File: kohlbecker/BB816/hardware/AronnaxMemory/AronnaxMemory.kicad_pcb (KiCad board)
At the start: 2 copper layers, 19 parts, among them J1 Barrel_Jack_Switch, J2 Conn_02x40_Odd_Even, J3 Conn_02x18_Odd_Even, J4 Conn_02x16_Odd_Even, U1 74LS04, U11 AS6C4008-55PCN, U12 AS6C4008-55PCN, U13 AT28C256-15PC, U2 74LS32, U3 74LS32, U4 74LS32, U5 74LS08, U6 74LS138, U7 74LS138, U8 74LS138

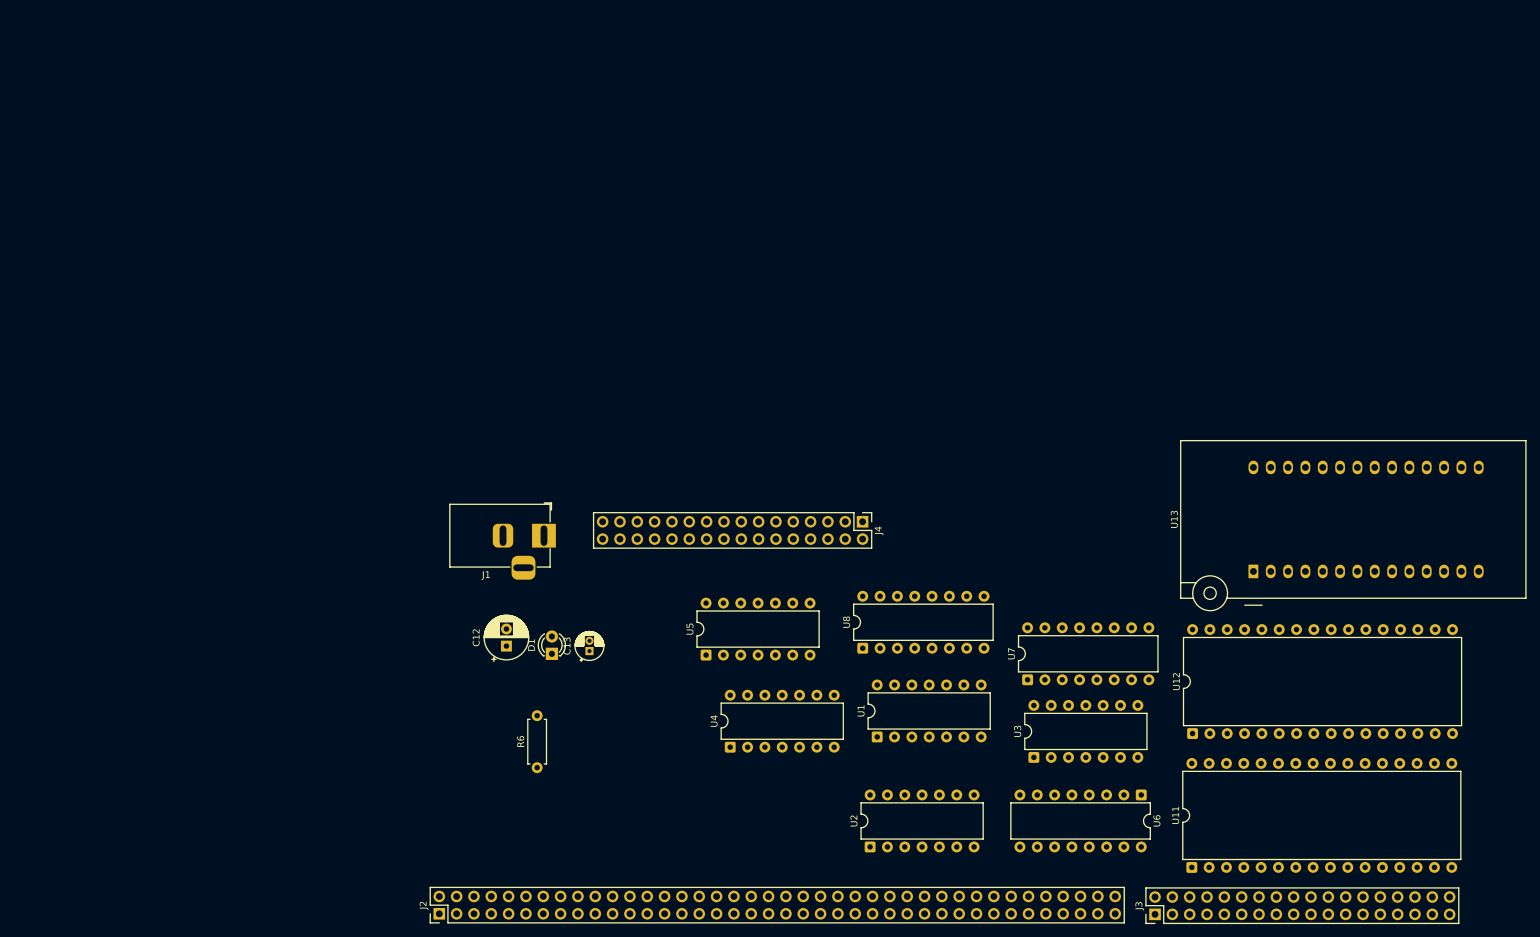
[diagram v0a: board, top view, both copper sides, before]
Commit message: Ready update schematic with added components to breakout
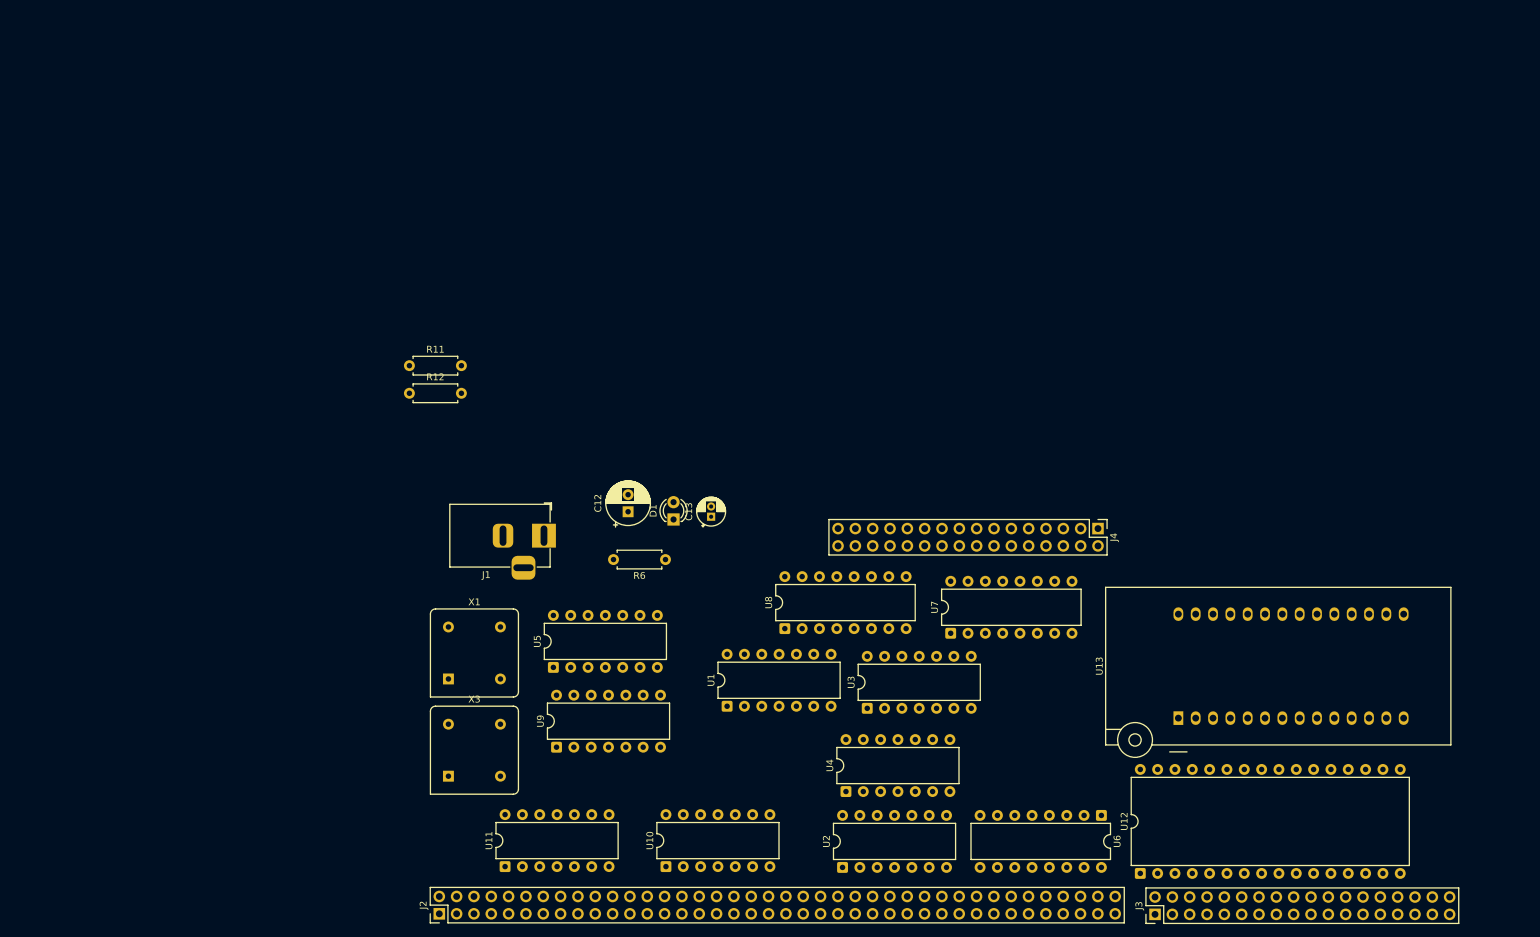
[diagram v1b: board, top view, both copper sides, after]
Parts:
- added R11: 3.3k, Resistor_THT:R_Axial_DIN0207_L6.3mm_D2.5mm_P7.62mm_Horizontal, F.Cu at (58.3, 49.6)
- added R12: 100k, Resistor_THT:R_Axial_DIN0207_L6.3mm_D2.5mm_P7.62mm_Horizontal, F.Cu at (58.3, 53.6)
- added U10: 74AHC125, Package_DIP:DIP-14_W7.62mm, F.Cu at (95.9, 123.0)
- added U9: 74HC74, Package_DIP:DIP-14_W7.62mm, F.Cu at (79.8, 105.5)
- added X1: 8MHz, Oscillator:Oscillator_DIP-8, F.Cu at (64.0, 95.5)
- added X3: 16MHz, Oscillator:Oscillator_DIP-8, F.Cu at (64.0, 109.8)
- U11: value AS6C4008-55PCN -> 74LS32; footprint Package_DIP:DIP-32_W15.24mm -> Package_DIP:DIP-14_W7.62mm
- U4: value 74LS32 -> 74LS08
- U5: value 74LS08 -> 74LS32
- moved U11 100.7 mm to (72.3, 123.0)
- moved R6 35.8 mm to (95.8, 78.0), turned to 180 degrees
- moved J4 34.5 mm to (159.2, 73.5)
- moved C12 26.6 mm to (90.3, 71.0)
- moved C13 26.6 mm to (102.5, 71.7)
- moved D1 26.6 mm to (97.0, 72.1)
- moved U3 25.5 mm to (125.4, 99.8)
- moved U13 24.2 mm to (171.0, 101.2)
- moved U1 22.5 mm to (104.8, 99.5)
- moved U5 22.5 mm to (79.4, 93.8)
- moved U12 21.9 mm to (165.4, 124.0)
- moved U4 18.2 mm to (122.3, 112.0)
- moved U7 13.2 mm to (137.6, 88.8)
- moved U8 11.8 mm to (113.3, 88.1)
- moved U6 6.57 mm to (159.7, 115.5)
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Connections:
- J4 pad 1: ~{MEG0} -> ~{MEG0_LO}
- J4 pad 3: MEG0 -> MEG0_LO
- J4 pad 5: ~{MEG0_HI} -> unconnected-(J4-Pin_5-Pad5)
- J4 pad 7: ~{MEG0_LO} -> unconnected-(J4-Pin_7-Pad7)
- U1 pad 1: /A19 -> ~{MEG0_LO}
- U1 pad 12: MEG0 -> Net-(X3-EN)
- U1 pad 13: ~{MEG0} -> /E
- U1 pad 2: Net-(U1-Pad2) -> MEG0_LO
- U1 pad 3: /A15 -> /E
- U1 pad 5: /E -> /A15
- U11 pad 1: /A18 -> /16MHz
- U11 pad 10: /A2 -> (no net)
- U11 pad 11: /A1 -> (no net)
- U11 pad 12: /A0 -> (no net)
- U11 pad 13: /D0 -> (no net)
- U11 pad 14: /D1 -> (no net)
- U11 pad 2: /A16 -> /8MHz
- U11 pad 3: /A14 -> Net-(U9B-C)
- U11 pad 4: /A12 -> (no net)
- U11 pad 5: /A7 -> (no net)
- U11 pad 6: /A6 -> (no net)
- U11 pad 7: /A5 -> (no net)
- U11 pad 8: /A4 -> (no net)
- U11 pad 9: /A3 -> (no net)
- U12 pad 22: ~{MEG0LO} -> ~{MEG0_LO}
- U2 pad 11: ~{MEG0HI} -> ~{MEG0_LO}
- U2 pad 12: ~{MEG0} -> Net-(U2-Pad12)
- U2 pad 13: Net-(U1-Pad2) -> /A19
- U2 pad 8: ~{MEG0} -> Net-(U2-Pad12)
- U3 pad 1: ~{MEG0} -> Net-(U1-Pad4)
- U3 pad 10: ~{BANK0_HI} -> /A15
- U3 pad 11: ~{BANK0_LO} -> Net-(U12-OE#)
- U3 pad 12: /~{BANK0} -> Net-(U3-Pad12)
- U3 pad 13: /A15 -> Net-(U1-Pad10)
- U3 pad 2: /A19 -> ~{BANK0_HI}
- U3 pad 3: ~{MEG0LO} -> ~{ROM_OE}
- U3 pad 4: Net-(U1-Pad4) -> Net-(U1-Pad6)
- U3 pad 8: ~{ROM_OE} -> ~{BANK0_LO}
- U3 pad 9: Net-(U1-Pad6) -> /~{BANK0}
- U4 pad 1: Net-(U4-Pad1) -> Net-(U1-Pad8)
- U4 pad 2: Net-(U1-Pad10) -> /E
- U4 pad 3: Net-(U12-OE#) -> Net-(U3-Pad12)
- U5 pad 1: Net-(U1-Pad8) -> (no net)
- U5 pad 2: /E -> (no net)
- U5 pad 3: Net-(U4-Pad1) -> (no net)

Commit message: getting ready to add VPB rewrite
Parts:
- removed J4: Conn_02x16_Odd_Even, Connector_PinHeader_2.54mm:PinHeader_2x16_P2.54mm_Vertical
- removed R11: 3.3k, Resistor_THT:R_Axial_DIN0207_L6.3mm_D2.5mm_P7.62mm_Horizontal
- removed R12: 100k, Resistor_THT:R_Axial_DIN0207_L6.3mm_D2.5mm_P7.62mm_Horizontal
- removed U10: 74AHC125, Package_DIP:DIP-14_W7.62mm
- removed U11, U5: 74LS32, Package_DIP:DIP-14_W7.62mm
- removed U9: 74HC74, Package_DIP:DIP-14_W7.62mm
- removed X1: 8MHz, Oscillator:Oscillator_DIP-8
- removed X3: 16MHz, Oscillator:Oscillator_DIP-8
- added C1: 100nF, Capacitor_THT:C_Disc_D3.4mm_W2.1mm_P2.50mm, F.Cu at (46.5, 76.0)
- added C2: 100nF, Capacitor_THT:C_Disc_D3.4mm_W2.1mm_P2.50mm, F.Cu at (78.8, 112.1)
- added C3: 100nF, Capacitor_THT:C_Disc_D3.4mm_W2.1mm_P2.50mm, F.Cu at (78.4, 68.5)
- added C4: 100nF, Capacitor_THT:C_Disc_D3.4mm_W2.1mm_P2.50mm, F.Cu at (119.0, 88.4)
- added C5: 100nF, Capacitor_THT:C_Disc_D3.4mm_W2.1mm_P2.50mm, F.Cu at (111.2, 68.0)
- added C6: 100nF, Capacitor_THT:C_Disc_D3.4mm_W2.1mm_P2.50mm, F.Cu at (78.1, 93.5)
- added C7: 100nF, Capacitor_THT:C_Disc_D3.4mm_W2.1mm_P2.50mm, F.Cu at (80.5, 80.9)
- added C8: 100nF, Capacitor_THT:C_Disc_D3.4mm_W2.1mm_P2.50mm, F.Cu at (105.8, 89.0)
- added C9: 100nF, Capacitor_THT:C_Disc_D3.4mm_W2.1mm_P2.50mm, F.Cu at (105.7, 68.0)
- added H1: MountingHole_Pad, MountingHole:MountingHole_3.2mm_M3_Pad, F.Cu at (30.5, 71.1)
- added H2: MountingHole_Pad, MountingHole:MountingHole_3.2mm_M3_Pad, F.Cu at (172.7, 71.1)
- added J5: I/O ~{CS}, Connector_PinHeader_2.54mm:PinHeader_2x10_P2.54mm_Vertical, F.Cu at (75.0, 68.4)
- added REF**: Symbol_Barrel_Polarity, Symbol:Symbol_Barrel_Polarity, F.Cu at (32.2, 88.9)
- J2, J3: moved to B.Cu
- U6, U7: value 74LS138 -> 74LS32; footprint Package_DIP:DIP-16_W7.62mm -> Package_DIP:DIP-14_W7.62mm
- moved U6 76.1 mm to (98.1, 70.9), turned to 0 degrees
- moved U12 65.6 mm to (114.1, 83.2)
- moved U8 63.9 mm to (49.6, 83.6)
- moved D1 57.2 mm to (41.8, 87.3), turned to 0 degrees
- moved C13 55.6 mm to (47.0, 68.9), turned to 0 degrees
- moved U4 55.3 mm to (78.3, 78.5)
- moved C12 53.3 mm to (37.1, 71.1), turned to 0 degrees
- moved U13 52.6 mm to (119.0, 109.3)
- moved R6 52.5 mm to (43.4, 75.0), turned to 90 degrees
- moved U3 48.1 mm to (78.1, 90.9)
- moved U2 43.0 mm to (78.8, 122.2)
- moved U7 39.9 mm to (97.9, 91.9), turned to 0 degrees
- moved J1 39.1 mm to (39.4, 80.6)
- moved J3 35.6 mm to (132.1, 127.0), turned to -90 degrees
- moved J2 34.8 mm to (27.9, 127.0), turned to -90 degrees
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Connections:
- net ~{ROM_OE} renamed /~{ROM_OE}
- J3 pad 11: /A4 -> /AA4
- J3 pad 13: /A3 -> /AA3
- J3 pad 15: /A2 -> /AA2
- J3 pad 17: /A1 -> /AA1
- U1 pad 1: ~{MEG0_LO} -> /E
- U1 pad 11: ~{PAGE1} -> /A19
- U1 pad 12: Net-(X3-EN) -> Net-(U1-Pad12)
- U1 pad 13: /E -> ~{PAGE1}
- U1 pad 2: MEG0_LO -> Net-(U1-Pad2)
- U1 pad 3: /E -> /~{BANK0_HI}
- U1 pad 8: Net-(U1-Pad8) -> unconnected-(U1-Pad8)
- U1 pad 9: ~{BANK0_HI} -> GND
- U12 pad 22: ~{MEG0_LO} -> /~{MEG0_LO}
- U13 pad 20: ~{BANK0_HI} -> /~{BANK0_HI}
- U2 pad 10: Net-(U2-Pad10) -> /A19
- U2 pad 11: ~{MEG0_LO} -> Net-(U2-Pad11)
- U2 pad 13: /A19 -> Net-(U2-Pad13)
- U2 pad 3: Net-(U2-Pad3) -> Net-(U2-Pad13)
- U2 pad 6: Net-(U2-Pad10) -> Net-(U2-Pad12)
- U2 pad 8: Net-(U2-Pad12) -> /~{MEG0_LO}
- U2 pad 9: Net-(U2-Pad3) -> Net-(U2-Pad11)
- U3 pad 1: Net-(U1-Pad4) -> Net-(U1-Pad2)
- U3 pad 13: Net-(U1-Pad10) -> Net-(U1-Pad12)
- U3 pad 2: ~{BANK0_HI} -> /~{BANK0_HI}
- U3 pad 6: ~{BANK0_HI} -> /~{BANK0_HI}
- U3 pad 8: ~{BANK0_LO} -> /~{BANK0_LO}
- U4 pad 1: Net-(U1-Pad8) -> GND
- U4 pad 10: (no net) -> GND
- U4 pad 11: (no net) -> unconnected-(U4-Pad11)
- U4 pad 12: (no net) -> GND
- U4 pad 13: (no net) -> GND
- U4 pad 2: /E -> GND
- U4 pad 3: Net-(U3-Pad12) -> unconnected-(U4-Pad3)
- U4 pad 4: (no net) -> Net-(U1-Pad4)
- U4 pad 5: (no net) -> /E
- U4 pad 6: (no net) -> Net-(U3-Pad12)
- U4 pad 8: (no net) -> unconnected-(U4-Pad8)
- U4 pad 9: (no net) -> GND
- U6 pad 1: /A11 -> /~{BANK0_LO}
- U6 pad 10: unconnected-(U6-O5-Pad10) -> Net-(U6-Pad10)
- U6 pad 11: unconnected-(U6-O4-Pad11) -> ~{MEG0_HI}
- U6 pad 12: unconnected-(U6-O3-Pad12) -> Net-(U1-Pad10)
- U6 pad 13: unconnected-(U6-O2-Pad13) -> Net-(U2-Pad11)
- U6 pad 14: unconnected-(U6-O1-Pad14) -> VCC
- U6 pad 2: /A12 -> /A8
- U6 pad 3: /A13 -> Net-(U6-Pad10)
- U6 pad 4: ~{BANK0_LO} -> /A9
- U6 pad 5: /A14 -> /A10
- U6 pad 6: VCC -> Net-(U6-Pad6)
- U6 pad 7: unconnected-(U6-O7-Pad7) -> GND
- U6 pad 8: unconnected-(U6-GND-Pad8) -> Net-(U6-Pad8)
- U6 pad 9: unconnected-(U6-O6-Pad9) -> Net-(U6-Pad6)
- U7 pad 1: /A8 -> /A11
- U7 pad 10: unconnected-(U7-O5-Pad10) -> Net-(U7-Pad10)
- U7 pad 11: unconnected-(U7-O4-Pad11) -> Net-(U7-Pad10)
- U7 pad 12: unconnected-(U7-O3-Pad12) -> Net-(U7-Pad12)
- U7 pad 13: unconnected-(U7-O2-Pad13) -> Net-(U7-Pad13)
- U7 pad 14: ~{PAGE1} -> VCC
- U7 pad 2: /A9 -> /A12
- U7 pad 3: /A10 -> Net-(U7-Pad13)
- U7 pad 4: Net-(U6-O0) -> /A13
- U7 pad 5: /A11 -> /A14
- U7 pad 6: VCC -> Net-(U7-Pad12)
- U7 pad 7: unconnected-(U7-O7-Pad7) -> GND
- U7 pad 8: unconnected-(U7-GND-Pad8) -> ~{PAGE1}
- U7 pad 9: unconnected-(U7-O6-Pad9) -> Net-(U6-Pad8)
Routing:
- added copper zone on In1.Cu, net GND
- added copper zone on In2.Cu, net GND
- added copper zone on B.Cu, net VCC
- added copper zone on F.Cu, net VCC
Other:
- board outline added: 152.4 x 64.8 mm
- copper layers 2 -> 4
- board text added: "+"
- board text added: "+5V"
- board text added: "-"
- board text added: "5V"
- board text added: "A0"
- board text added: "A1"
- board text added: "A10"
- board text added: "A11"
- board text added: "A12"
- board text added: "A13"
- board text added: "A14"
- board text added: "A15"
- board text added: "A16"
- board text added: "A17"
- board text added: "A18"
- board text added: "A19"
- board text added: "A2"
- board text added: "A20"
- board text added: "A21"
- board text added: "A22"
- board text added: "A23"
- board text added: "A3"
- board text added: "A4"
- board text added: "A5"
- board text added: "A6"
- board text added: "A7"
- board text added: "A8"
- board text added: "A9"
- board text added: "BE"
- board text added: "CLK"
- board text added: "CLK_SRC"
- board text added: "D0"
- board text added: "D1"
- board text added: "D2"
- board text added: "D3"
- board text added: "D4"
- board text added: "D5"
- board text added: "D6"
- board text added: "D7"
- board text added: "E"
- board text added: "GND"
- board text added: "M"
- board text added: "RDY_IN"
- board text added: "RST"
- board text added: "R~{W}"
- board text added: "SYNC"
- board text added: "VA"
- board text added: "X"
- board text added: "~{00}"
- board text added: "~{20}"
- board text added: "~{40}"
- board text added: "~{512K_1}"
- board text added: "~{60}"
- board text added: "~{80}"
- board text added: "~{A0}"
- board text added: "~{ABORT}"
- board text added: "~{BANK0}"
- board text added: "~{C0}"
- board text added: "~{CLK"
- board text added: "~{CLK_EN}"
- board text added: "~{E0}"
- board text added: "~{IRQ}"
- board text added: "~{ML}"
- board text added: "~{MR}⎒"
- board text added: "~{NMI}"
- board text added: "~{PAGE_1}"
- board text added: "~{RD}"
- board text added: "~{RST}"
- board text added: "~{VP}"
- board text added: "~{WAI}"
- board text added: "~{WR}"

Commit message: Memory
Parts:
- added J9: Vector Rewrite, Connector_PinHeader_2.54mm:PinHeader_2x11_P2.54mm_Vertical, B.Cu at (127.1, 118.0)
- moved U1 36.6 mm to (87.9, 68.4), turned to 0 degrees
- moved C6 32.2 mm to (98.0, 68.2), turned to -90 degrees
- moved C9 28.3 mm to (88.0, 90.2), turned to -90 degrees
- moved U6 27.9 mm to (90.9, 97.8), turned to 90 degrees
- moved C13 27.5 mm to (39.1, 95.3)
- moved R6 27.5 mm to (35.5, 101.3)
- moved C12 27.5 mm to (29.2, 97.4)
- moved U3 26.8 mm to (104.6, 86.8)
- moved U4 26.4 mm to (104.6, 75.8)
- moved C3 23.3 mm to (101.7, 68.0), turned to -90 degrees
- moved C8 21.9 mm to (88.0, 101.8), turned to -90 degrees
- moved C7 21.2 mm to (101.7, 79.2), turned to -90 degrees
- moved U7 19.1 mm to (90.9, 109.7), turned to 90 degrees
- moved U13 15.9 mm to (134.9, 109.1)
- moved C4 15.7 mm to (134.7, 88.8)
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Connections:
- U3 pad 1: Net-(U1-Pad2) -> Net-(U1-Pad6)
- U3 pad 2: /~{BANK0_HI} -> /~{BANK0}
- U3 pad 3: /~{ROM_OE} -> /~{BANK0_HI}
- U3 pad 4: Net-(U1-Pad6) -> Net-(U1-Pad2)
- U3 pad 5: /~{BANK0} -> /~{BANK0_HI}
- U3 pad 6: /~{BANK0_HI} -> /~{ROM_OE}
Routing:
- net /A10: track 0.00 -> 88.7 mm, vias 0 -> 1
- net /A14: track 0.00 -> 82.0 mm, vias 0 -> 1
- net /~{MEG0_LO}: track 0.00 -> 79.0 mm
- net /A9: track 0.00 -> 75.1 mm
- net /A11: track 0.00 -> 74.5 mm, vias 0 -> 1
- net /A13: track 0.00 -> 67.8 mm, vias 0 -> 1
- net /A17: track 0.00 -> 66.6 mm
- net /D3: track 0.00 -> 65.8 mm
- net /A8: track 0.00 -> 62.5 mm
- net /D4: track 0.00 -> 60.4 mm
- net /D7: track 0.00 -> 60.2 mm
- net /D5: track 0.00 -> 60.0 mm
- net /D6: track 0.00 -> 59.9 mm
- net /A0: track 0.00 -> 53.7 mm
- net /E: track 0.00 -> 52.6 mm
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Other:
- board text added: "~{$80000}"
- board text added: "~{0100}"
- board text removed: "~{512K_1}"
- board text removed: "~{PAGE_1}"

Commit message: Cleanup
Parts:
- removed C6, C8: 100nF, Capacitor_THT:C_Disc_D3.4mm_W2.1mm_P2.50mm
- removed U2, U7: 74LS32, Package_DIP:DIP-14_W7.62mm
- removed U8: 74LS138, Package_DIP:DIP-16_W7.62mm
- added C10: 100nF, Capacitor_THT:C_Disc_D3.4mm_W2.1mm_P2.50mm, F.Cu at (121.5, 88.9)
- added C11: 100nF, Capacitor_THT:C_Disc_D3.4mm_W2.1mm_P2.50mm, F.Cu at (128.2, 67.5)
- added U10: 74HC30, Package_DIP:DIP-14_W7.62mm, F.Cu at (115.3, 91.8)
- added U9: CD4072B, Package_DIP:DIP-14_W7.62mm, F.Cu at (91.4, 119.6)
- moved C1 60.1 mm to (112.8, 91.5)
- moved C2 51.5 mm to (110.4, 67.4), turned to 180 degrees
- moved U1 27.6 mm to (102.7, 91.7)
- moved U6 27.3 mm to (90.6, 70.5), turned to 0 degrees
- moved C3 20.8 mm to (122.5, 67.4), turned to 180 degrees
- moved C9 19.6 mm to (91.3, 109.5), turned to 0 degrees
- moved U3 19.3 mm to (114.8, 70.5), turned to 0 degrees
- moved C7 12.3 mm to (98.3, 67.4), turned to 180 degrees
- moved J5 11.1 mm to (74.8, 76.1)
- moved U4 5.65 mm to (102.7, 70.5), turned to 0 degrees
- moved U12 1.48 mm to (128.4, 85.1)
- moved C5 1.48 mm to (125.6, 69.9)
- moved C4 1.28 mm to (135.1, 87.6), turned to 180 degrees
- moved U13 0.44 mm to (135.2, 108.8)
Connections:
- net /~{WR} renamed ~{WR}
- J5 pad 10: ~{0xA0} -> unconnected-(J5-Pin_10-Pad10)
- J5 pad 12: ~{0x80} -> unconnected-(J5-Pin_12-Pad12)
- J5 pad 14: ~{0x60} -> unconnected-(J5-Pin_14-Pad14)
- J5 pad 16: ~{0x40} -> unconnected-(J5-Pin_16-Pad16)
- J5 pad 18: ~{0x20} -> unconnected-(J5-Pin_18-Pad18)
- J5 pad 20: ~{0x00} -> unconnected-(J5-Pin_20-Pad20)
- J5 pad 6: ~{0xE0} -> unconnected-(J5-Pin_6-Pad6)
- J5 pad 8: ~{0xCO} -> unconnected-(J5-Pin_8-Pad8)
- J9 pad 15: Net-(J9-Pin_15) -> GND
- J9 pad 17: Net-(J9-Pin_15) -> GND
- J9 pad 19: Net-(J9-Pin_15) -> GND
- J9 pad 21: Net-(J9-Pin_15) -> GND
- U1 pad 1: /E -> /A15
- U1 pad 11: /A19 -> /E
- U1 pad 13: ~{PAGE1} -> ~{BANK0_HI}
- U1 pad 2: Net-(U1-Pad2) -> /~{A15}
- U1 pad 3: /~{BANK0_HI} -> PAGE1
- U1 pad 4: Net-(U1-Pad4) -> ~{PAGE1}
- U1 pad 5: /A15 -> GND
- U1 pad 6: Net-(U1-Pad6) -> unconnected-(U1-Pad6)
- U1 pad 8: unconnected-(U1-Pad8) -> /~{A19}
- U1 pad 9: GND -> /A19
- U12 pad 22: /~{MEG0_LO} -> ~{MEG0_LO}
- U12 pad 24: Net-(U12-OE#) -> ~{MEG0_LO_OE}
- U13 pad 20: /~{BANK0_HI} -> ~{BANK0_HI}
- U13 pad 22: /~{ROM_OE} -> unconnected-(U13-~{OE}-Pad22)
- U3 pad 1: Net-(U1-Pad6) -> /~{A15}
- U3 pad 10: /A15 -> PAGE1
- U3 pad 11: Net-(U12-OE#) -> /~{BANK0_LO}
- U3 pad 12: Net-(U3-Pad12) -> /~{BANK0}
- U3 pad 13: Net-(U1-Pad12) -> /A15
- U3 pad 3: /~{BANK0_HI} -> ~{BANK0_HI}
- U3 pad 4: Net-(U1-Pad2) -> Net-(U1-Pad10)
- U3 pad 5: /~{BANK0_HI} -> ~{BANK0_HI}
- U3 pad 6: /~{ROM_OE} -> ~{ROM_OE}
- U3 pad 8: /~{BANK0_LO} -> ~{MEG0_LO_OE}
- U3 pad 9: /~{BANK0} -> Net-(U3-Pad9)
- U4 pad 11: unconnected-(U4-Pad11) -> Net-(U3-Pad9)
- U4 pad 12: GND -> Net-(U1-Pad12)
- U4 pad 13: GND -> /E
- U4 pad 4: Net-(U1-Pad4) -> GND
- U4 pad 5: /E -> GND
- U4 pad 6: Net-(U3-Pad12) -> unconnected-(U4-Pad6)
- U6 pad 1: /~{BANK0_LO} -> /~{MEG0}
- U6 pad 10: Net-(U6-Pad10) -> GND
- U6 pad 12: Net-(U1-Pad10) -> /~{A19}
- U6 pad 13: Net-(U2-Pad11) -> /~{MEG0}
- U6 pad 2: /A8 -> /A19
- U6 pad 3: Net-(U6-Pad10) -> ~{MEG0_LO}
- U6 pad 4: /A9 -> GND
- U6 pad 5: /A10 -> GND
- U6 pad 6: Net-(U6-Pad6) -> unconnected-(U6-Pad6)
- U6 pad 8: Net-(U6-Pad8) -> unconnected-(U6-Pad8)
- U6 pad 9: Net-(U6-Pad6) -> GND
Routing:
- net ~{WR}: track 25.9 -> 134.9 mm
- net /A15: track 18.6 -> 110.9 mm, vias 0 -> 1
- net /~{BANK0}: track 0.00 -> 80.9 mm, vias 0 -> 2
- net /~{MEG0_LO}: track 79.0 -> 0.00 mm
- net /E: track 52.6 -> 127.1 mm
- net ~{BANK0_HI}: track 0.00 -> 67.5 mm
- net ~{MEG0_LO}: track 0.00 -> 66.5 mm
- net /~{MEG0}: track 0.00 -> 58.1 mm
- net /A19: track 15.0 -> 68.3 mm
- net PAGE1: track 0.00 -> 51.9 mm, vias 0 -> 2
- net Net-(U12-OE#): track 41.3 -> 0.00 mm
- net (no net): track 0.00 -> 39.9 mm
- net /~{A19}: track 0.00 -> 39.5 mm
- net Net-(U1-Pad10): track 0.00 -> 35.2 mm
- net ~{MEG0_LO_OE}: track 0.00 -> 32.8 mm
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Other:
- board text removed: "~{00}"
- board text removed: "~{20}"
- board text removed: "~{40}"
- board text removed: "~{60}"
- board text removed: "~{80}"
- board text removed: "~{A0}"
- board text removed: "~{C0}"
- board text removed: "~{E0}"
